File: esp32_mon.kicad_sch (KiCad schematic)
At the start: 31 parts, among them J1 I2C, J2 UART, J3 BAT, J4 USB, Q1 NTJD1155L, Q2 MMDT3904, U1 ESP32, U2 TC4054GR, U3 RT9080-33GJ5S, U4 SHT4x

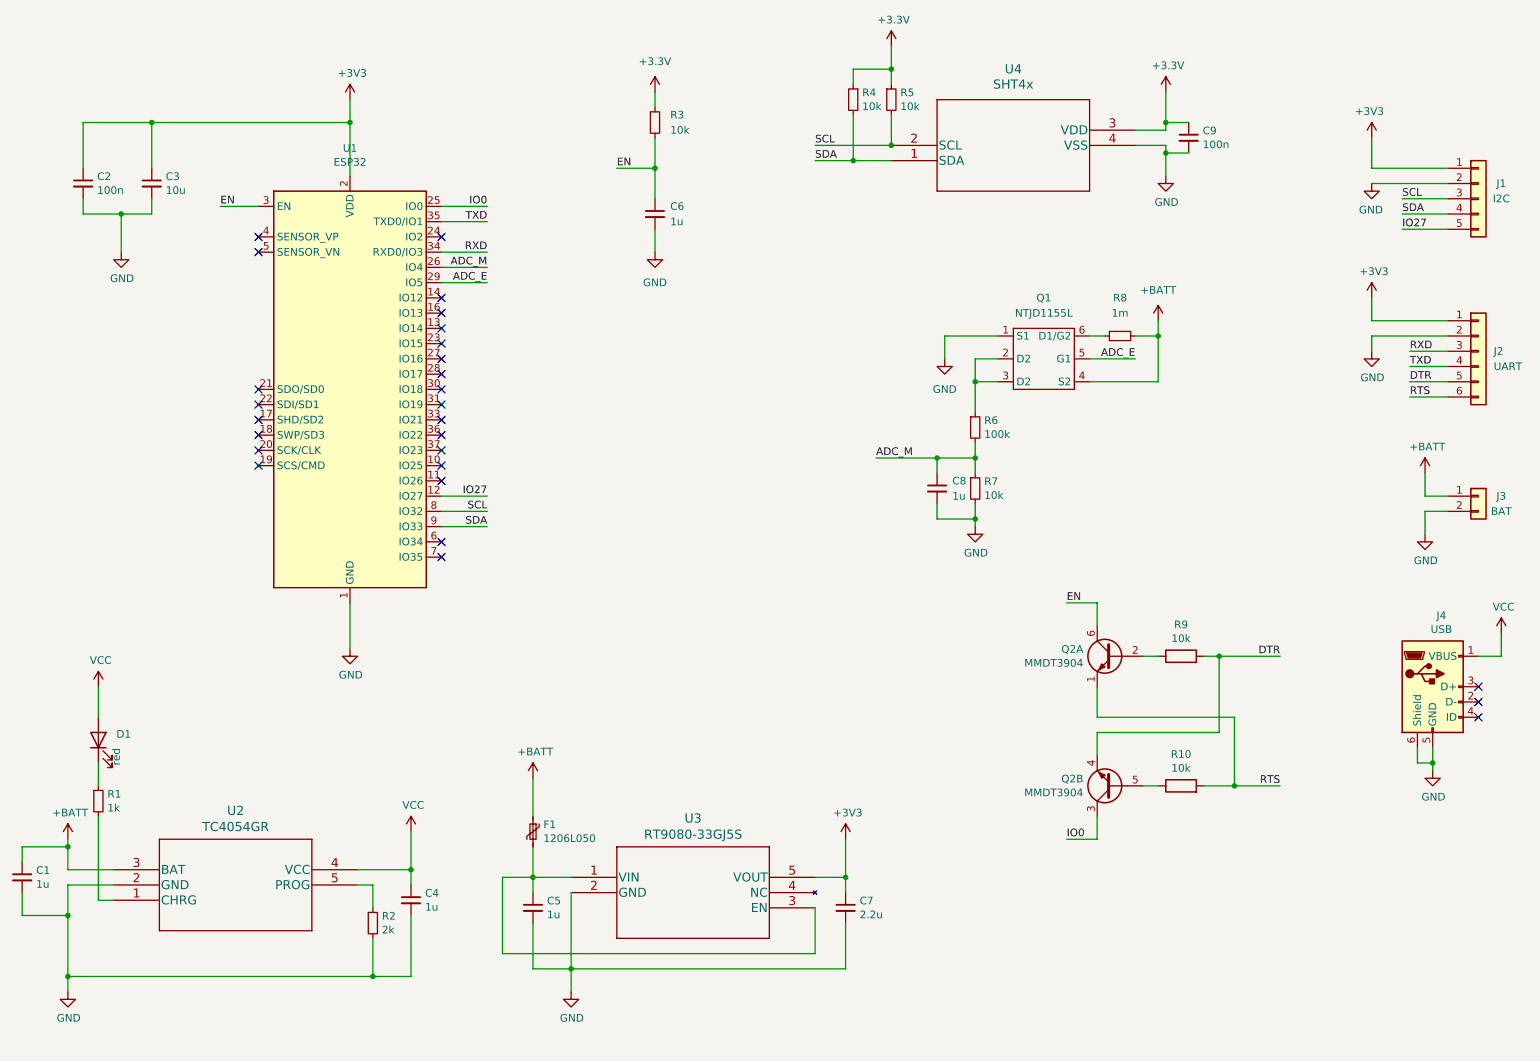
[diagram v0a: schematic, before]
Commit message: update to availabe parts and tweaks
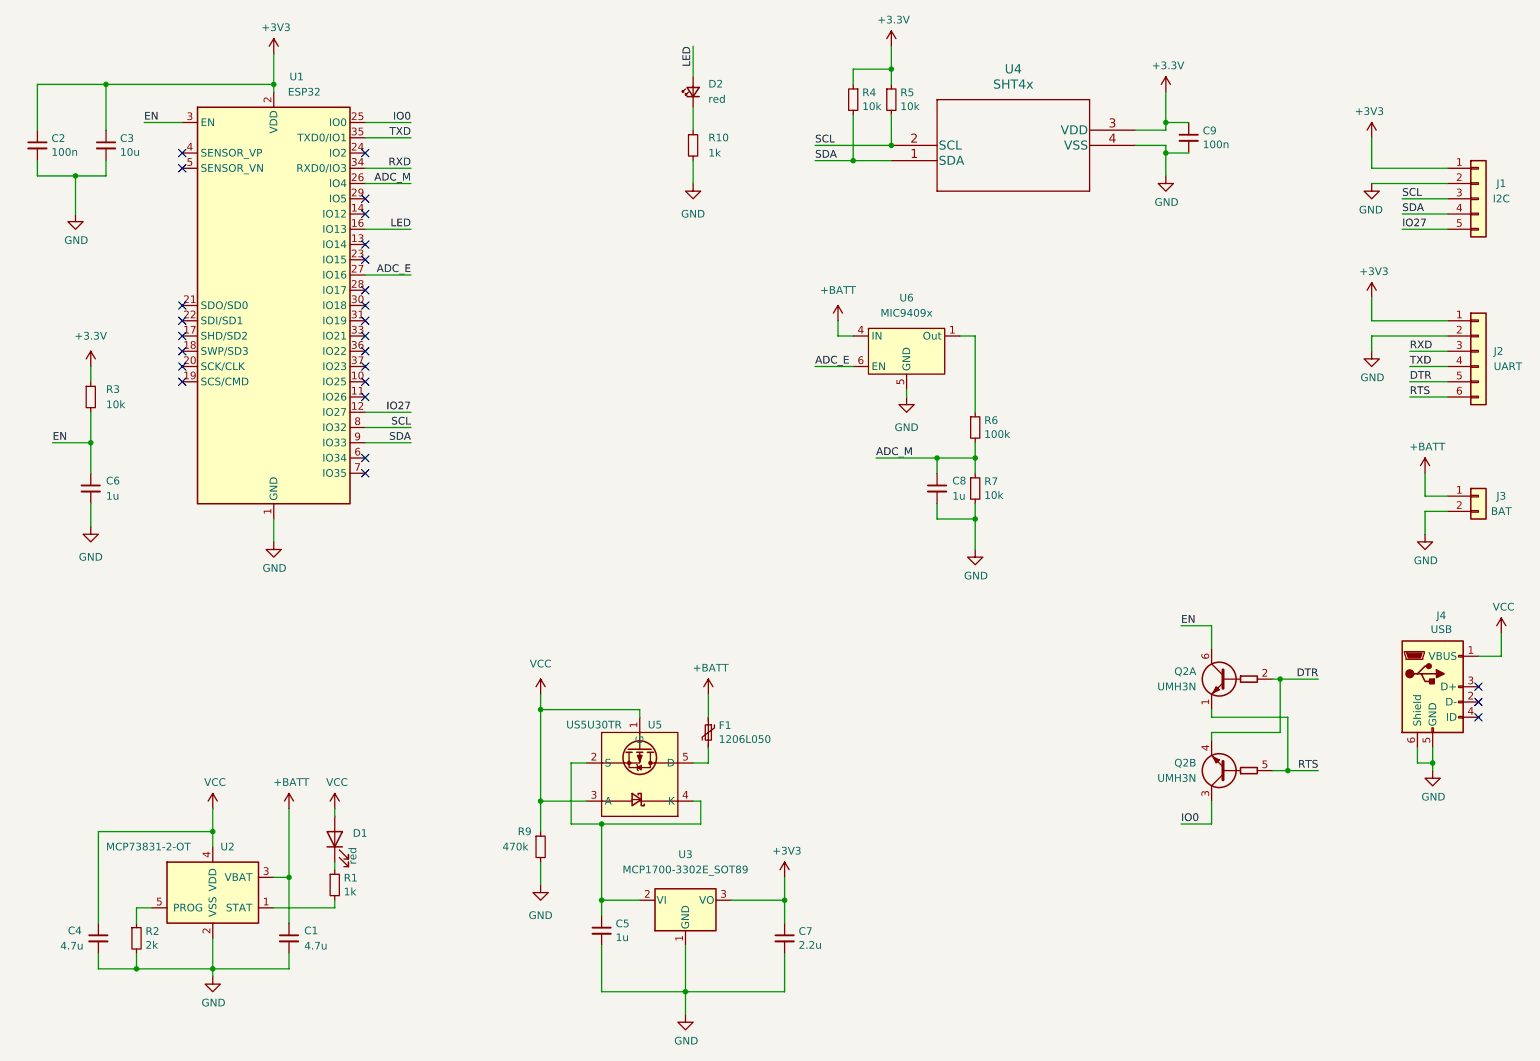
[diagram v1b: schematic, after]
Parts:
- removed Q1: NTJD1155L, Package_TO_SOT_SMD:SOT-363_SC-70-6_Handsoldering, symbol parts:NTJD1155L
- removed Q2: MMDT3904, Package_TO_SOT_SMD:SOT-363_SC-70-6_Handsoldering, symbol Transistor_BJT:MMDT3904
- removed R10, R9: 10k, Resistor_SMD:R_0805_2012Metric_Pad1.20x1.40mm_HandSolder, symbol Device:R
- removed R8: 1m, Resistor_SMD:R_0805_2012Metric_Pad1.20x1.40mm_HandSolder, symbol Device:R_Small
- removed U2: TC4054GR, Package_TO_SOT_SMD:TSOT-23-5_HandSoldering, symbol parts:STC4054GR
- removed U3: RT9080-33GJ5S, Package_TO_SOT_SMD:TSOT-23-5_HandSoldering, symbol parts:RT9080-33GJ5
- added D2: red, Diode_SMD:D_0805_2012Metric_Pad1.15x1.40mm_HandSolder, symbol Device:LED_Small
- added Q2: UMH3N, Package_TO_SOT_SMD:SOT-363_SC-70-6, symbol Transistor_BJT:UMH3N
- added R10: 1k, Resistor_SMD:R_0805_2012Metric_Pad1.20x1.40mm_HandSolder, symbol Device:R_Small
- added R9: 470k, Resistor_SMD:R_0805_2012Metric_Pad1.20x1.40mm_HandSolder, symbol Device:R_Small
- added U2: MCP73831-2-OT, Package_TO_SOT_SMD:SOT-23-5, symbol Battery_Management:MCP73831-2-OT
- added U3: MCP1700-3302E_SOT89, Package_TO_SOT_SMD:SOT-89-3, symbol Regulator_Linear:MCP1700-3302E_SOT89
- added U5: US5U30TR, Package_TO_SOT_SMD:SOT-353_SC-70-5, symbol parts:US5U30TR
- added U6: MIC9409x, Package_TO_SOT_SMD:SOT-363_SC-70-6, symbol parts:MIC9409x
- C1, C4: value 1u -> 4.7u
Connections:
- net +3V3: now also U3.3 (VO)
- net +BATT: now also U2.3 (VBAT), U6.4 (IN)
- net ADC_E: now also U1.27 (IO16), U6.6 (EN); no longer U1.29 (IO5)
- net DTR: now also Q2.2 (B1), Q2.4 (E2)
- net EN: now also Q2.6 (C1)
- net GND: now also R10.2, R9.2, U2.2 (VSS), U3.1 (GND), U6.2 (GND), U6.5 (GND)
- net IO0: now also Q2.3 (C2)
- net RTS: now also Q2.1 (E1), Q2.5 (B2)
- net VCC: now also R9.1, U2.4 (VDD), U5.1 (G), U5.3 (A)
- net LED: now reaches U1.16 (IO13)
- net LED: now also D2.2 (A)
- net at C5.1: now also U3.2 (VI), U5.2 (S), U5.4 (K); no longer F1.2
- net at R1.2: now also U2.1 (STAT)
- net at R2.1: now also U2.5 (PROG)
- net at R6.1: now also U6.1 (Out)
- new net: F1.2, U5.5 (D)
- new net: D2.1 (K), R10.1
- no-connect marks 27 -> 26
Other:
- moved on the sheet: C1, C2, C3, C4, C5, C6, C7, D1, F1, R1, R2, R3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
